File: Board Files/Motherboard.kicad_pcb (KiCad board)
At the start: 2 copper layers, 196.3 x 118.7 mm, 103 parts, among them P1 72-Pin Connector, P2 EXP-Connector, P3 MOD RF, P4 Controller Input, P5 Controller Input, P6 Alt PWR/RST IN, P6 PWR/RST IN, Q1 2SA937, Q2 2SC2021, Q3 2SC2021, U1 6116 (WRAM), U10 CIC, U2 74HC373, U3 74HC139, U4 6116 (VRAM), U5 RP2C02 PPU, U6 RP2A03 CPU, U7 40H368 (CI), U8 40H368 (CII), U9 74LS04, X1 21.477272 MHz, X2 4MHz

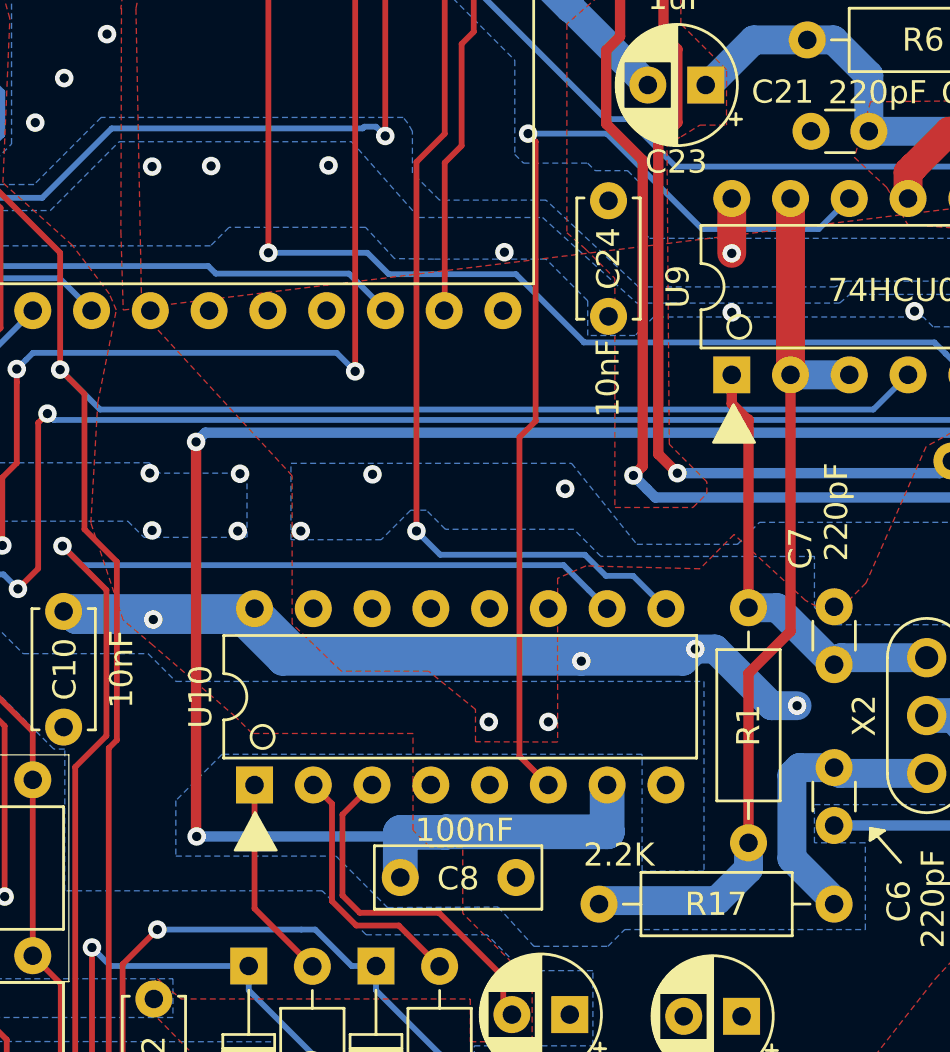
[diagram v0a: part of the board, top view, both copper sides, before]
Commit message: Added NullCIC
Added Redherring32's NullCIC design built into the main board instead of as a daughter board. You can choose to either populate the CIC or the capacitor, resistor, and IC under it.
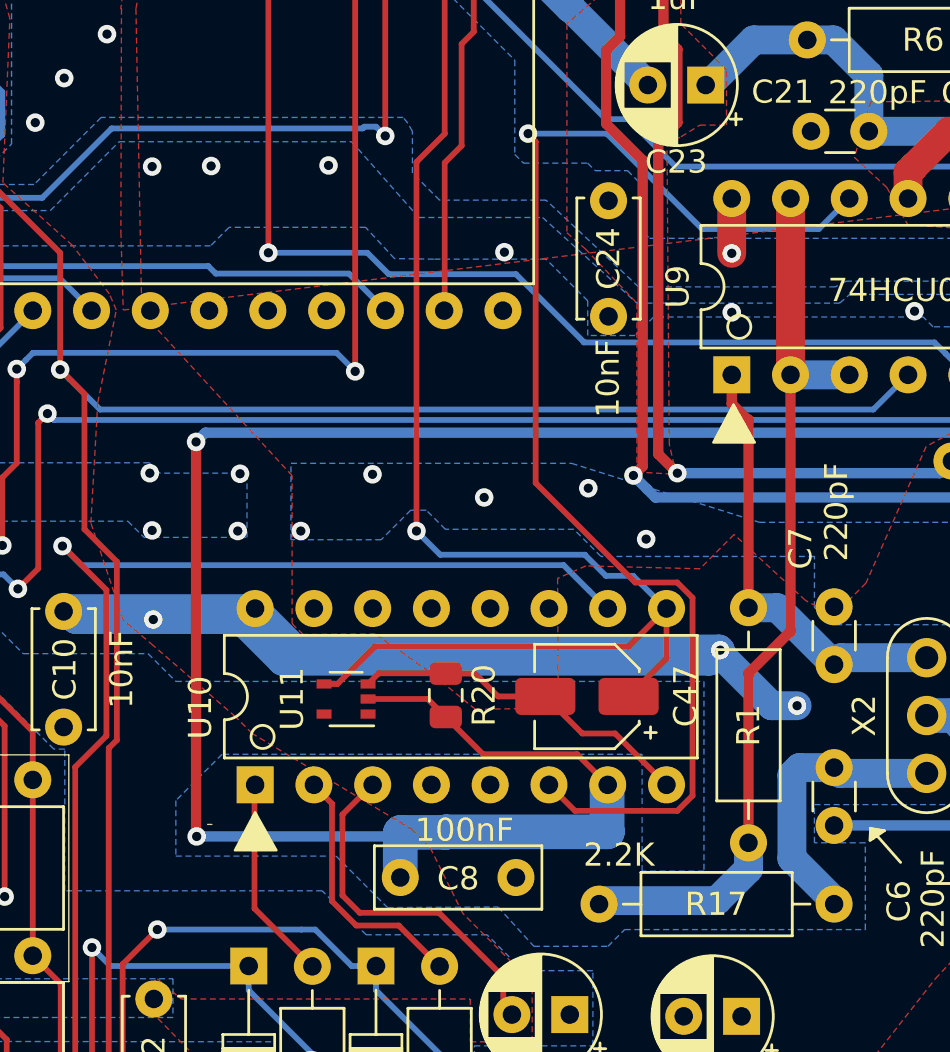
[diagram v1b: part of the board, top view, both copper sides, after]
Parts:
- added C47: 0.47uF, Capacitor_SMD:CP_Elec_4x5.3, F.Cu at (146.3, -38.3)
- added R20: 0R, Resistor_SMD:R_0805_2012Metric, F.Cu at (140.2, -38.4)
- added U11: , Package_TO_SOT_SMD:SOT-353_SC-70-5, F.Cu at (135.9, -38.2)
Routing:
- net /~{RST}: track 223.5 -> 244.1 mm
- net /GND: track 124.6 -> 139.7 mm
- net Net-(C17-Pad2): track 117.7 -> 129.6 mm
- net Net-(U10-Pad6): track 45.2 -> 55.7 mm
- net /VCC: track 246.1 -> 247.3 mm, vias 38 -> 37
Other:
- outline, holes or cut-outs redrawn
- board text added: "NullCIC"
